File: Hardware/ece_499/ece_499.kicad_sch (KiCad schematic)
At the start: 3 parts, among them U1 ESP32-C3_SUPERMINI, U2 ATA6561-GAQW-N, U3 AP62200WU-7

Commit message: Continue components selection and setup
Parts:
- removed U1: ESP32-C3_SUPERMINI, ESP32-C3_SUPERMINI:MODULE_ESP32-C3_SUPERMINI, symbol Imported_Parts:ESP32-C3_SUPERMINI
- added D1: B5817W, Diode_THT:D_DO-41_SOD81_P10.16mm_Horizontal, symbol Diode:1N5817
- added Q1, Q2, Q3, Q4: DMN2004WK, Package_TO_SOT_SMD:SOT-323_SC-70, symbol Transistor_FET:2N7002H
- added U1: Xiao ESP32-C3, Imported_Parts:XIAO ESP32-C3, symbol Imported_Parts:XIAO_ESP32-C3
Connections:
- net +5V: now reaches U2.3 (VCC)
- net +5V: now also D1.2 (A)
- new net: D1.1 (K), U1.8 (VUSB)
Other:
- moved on the sheet: U3

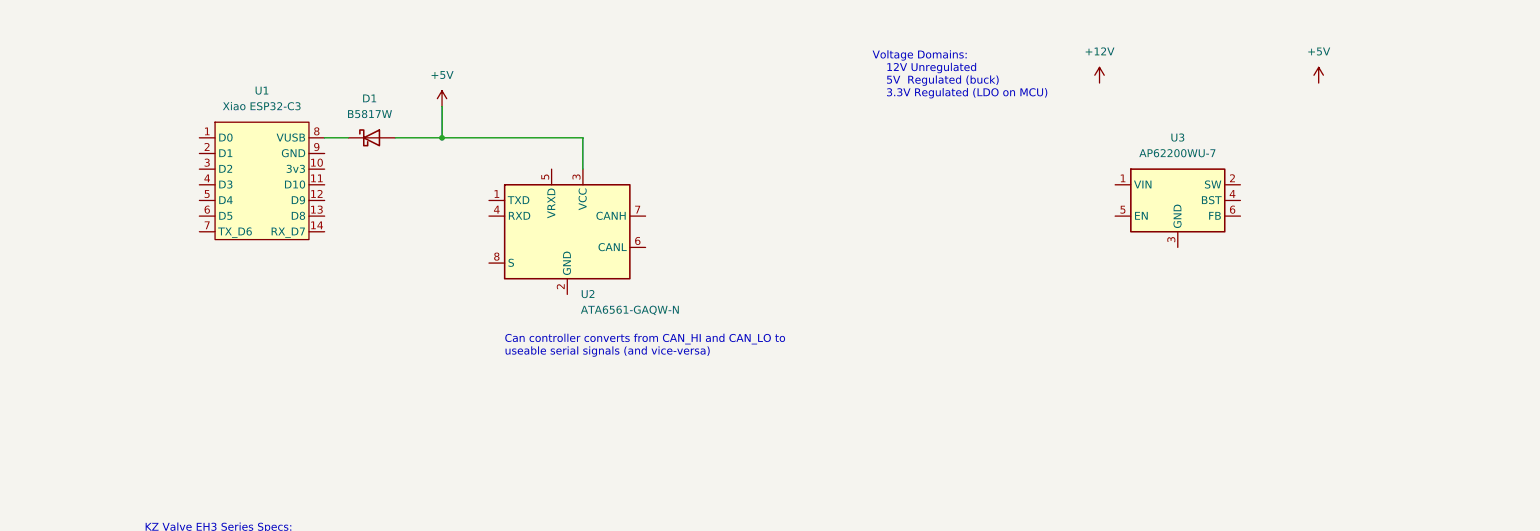
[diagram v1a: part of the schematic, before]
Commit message: Added parts
-Created circuit for regulator
-Wired up CAN transceiver
-Added rotary encoder
-Added I2C LCD interface
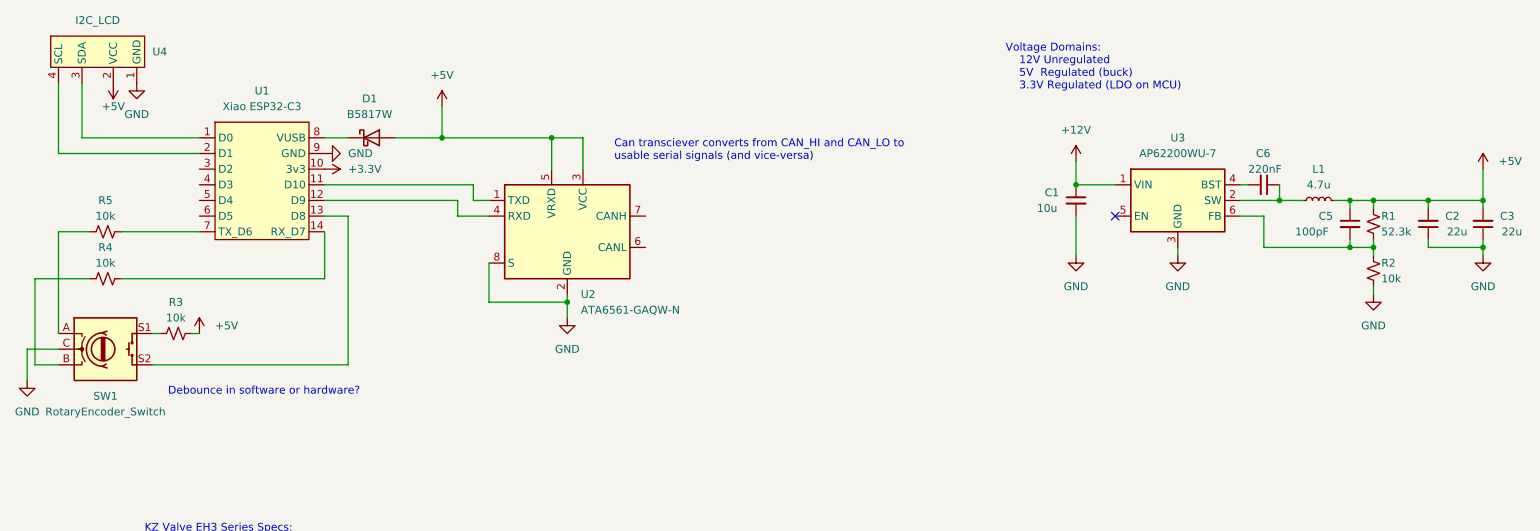
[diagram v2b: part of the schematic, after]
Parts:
- added C1: 10u, symbol Device:C_Small
- added C2, C3: 22u, symbol Device:C_Small
- added C5: 100pF, symbol Device:C_Small
- added C6: 220nF, symbol Device:C_Small
- added L1: 4.7u, symbol Device:L_Small
- added R1: 52.3k, symbol Device:R_Small_US
- added R2, R3, R4, R5: 10k, symbol Device:R_Small_US
- added SW1: RotaryEncoder_Switch, symbol Device:RotaryEncoder_Switch
- added U4: I2C_LCD, symbol Imported_Parts:I2C_LCD
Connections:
- net +12V: now also U3.1 (VIN), C1.1
- net +5V: now also U2.5 (VRXD), C2.2, C3.2, C5.1, L1.2, R1.1, R3.2, U4.2 (VCC)
- net at U1.1 (D0): now also U4.3 (SDA)
- net +3.3V: now reaches U1.10 (3v3)
- net at U1.11 (D10): now also U2.1 (TXD)
- net at U1.12 (D9): now also U2.4 (RXD)
- net at U1.13 (D8): now also SW1.S2
- net at U1.14 (RX_D7): now also R4.2
- net at U1.2 (D1): now also U4.4 (SCL)
- net at U1.7 (TX_D6): now also R5.2
- net GND: now reaches U1.9 (GND)
- net GND: now also U2.2 (GND), U2.8 (S), U3.3 (GND), C1.2, C2.1, C3.1, R2.2, SW1.C, U4.1 (GND)
- net at U3.2 (SW): now also C6.1, L1.1
- net at U3.4 (BST): now also C6.2
- net at U3.6 (FB): now also C5.2, R1.2, R2.1
- new net: R5.1, SW1.A
- new net: R3.1, SW1.S1
- new net: R4.1, SW1.B
- no-connect marks 0 -> 1
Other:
- note added: "Can transciever converts from CAN_HI and CAN_LO to usable serial signals (and vice-versa)"
- note added: "Debounce in software or hardware?"
- note removed: "Can controller converts from CAN_HI and CAN_LO to useable serial signals (and vice-versa)"

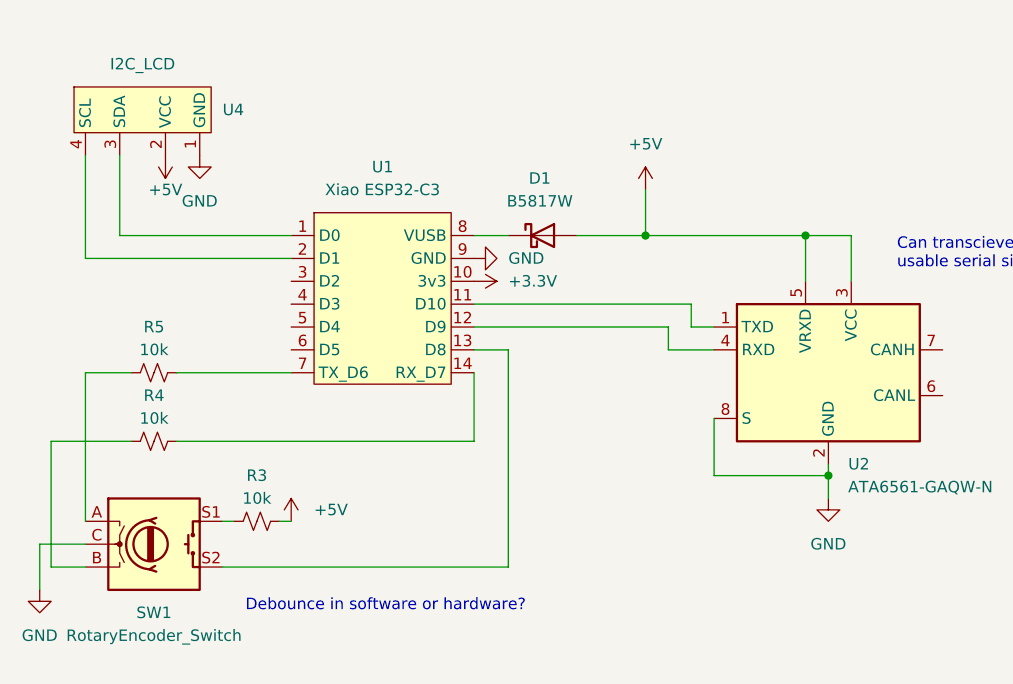
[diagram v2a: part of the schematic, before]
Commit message: stop being dumb
-fixed 5v into switch and can transceiver
-made the symbol less bad for the i2c
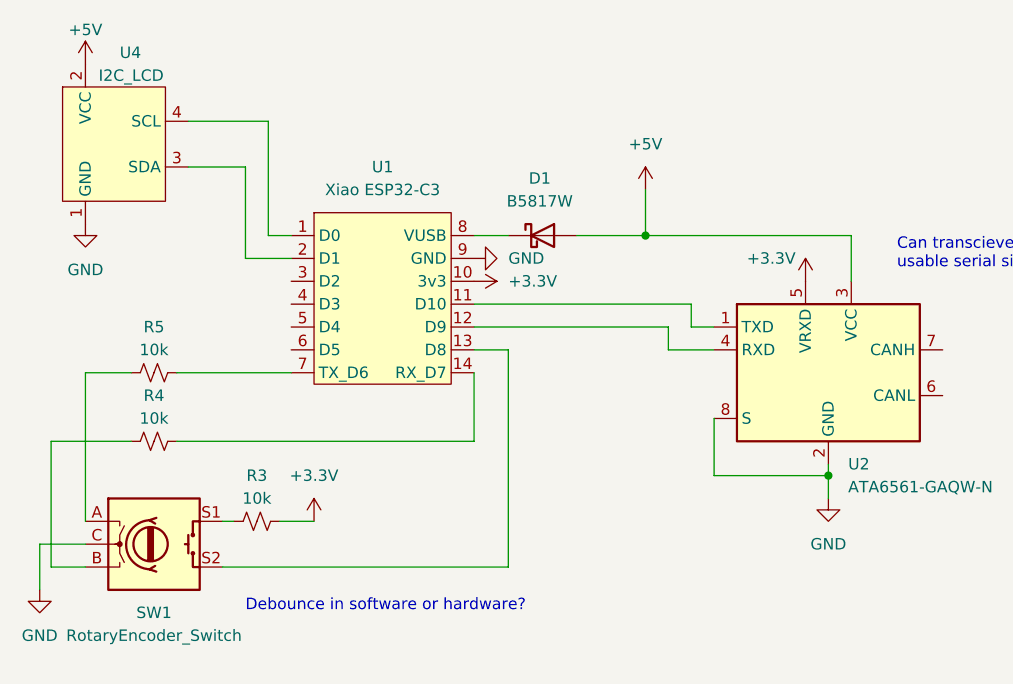
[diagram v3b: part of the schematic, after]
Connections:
- net +3.3V: now also R3.2, U2.5 (VRXD)
- net +5V: no longer R3.2, U2.5 (VRXD)
- net at U1.1 (D0): now also U4.4 (SCL); no longer U4.3 (SDA)
- net at U1.2 (D1): now also U4.3 (SDA); no longer U4.4 (SCL)
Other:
- moved on the sheet: U4
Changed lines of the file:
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@@
   (junction (at 224.79 53.34) (diameter 0) (color 0 0 0 0)
-  )
-  (junction (at 106.68 43.18) (diameter 0) (color 0 0 0 0)
   )
   (junction (at 240.03 60.96) (diameter 0) (color 0 0 0 0)
@@
     (stroke (width 0) (type default))
   )
-  (wire (pts (xy 88.9 43.18) (xy 106.68 43.18))
+  (wire (pts (xy 88.9 43.18) (xy 111.76 43.18))
+    (stroke (width 0) (type default))
+  )
+  (wire (pts (xy 44.45 45.72) (xy 49.53 45.72))
     (stroke (width 0) (type default))
   )
@@
     (stroke (width 0) (type default))
   )
+  (wire (pts (xy 44.45 35.56) (xy 44.45 45.72))
+    (stroke (width 0) (type default))
+  )
   (wire (pts (xy 69.85 43.18) (xy 73.66 43.18))
     (stroke (width 0) (type default))
@@
     (stroke (width 0) (type default))
   )
+  (wire (pts (xy 46.99 43.18) (xy 49.53 43.18))
+    (stroke (width 0) (type default))
+  )
   (wire (pts (xy 248.92 60.96) (xy 257.81 60.96))
     (stroke (width 0) (type default))
@@
     (stroke (width 0) (type default))
   )
-  (wire (pts (xy 30.48 34.29) (xy 30.48 43.18))
+  (wire (pts (xy 38.1 35.56) (xy 44.45 35.56))
     (stroke (width 0) (type default))
   )
@@
     (stroke (width 0) (type default))
   )
-  (wire (pts (xy 106.68 43.18) (xy 111.76 43.18))
-    (stroke (width 0) (type default))
-  )
   (wire (pts (xy 91.44 53.34) (xy 69.85 53.34))
     (stroke (width 0) (type default))
   )
-  (wire (pts (xy 26.67 45.72) (xy 49.53 45.72))
-    (stroke (width 0) (type default))
-  )
   (wire (pts (xy 257.81 60.96) (xy 257.81 59.69))
     (stroke (width 0) (type default))
@@
     (stroke (width 0) (type default))
   )
-  (wire (pts (xy 49.53 74.93) (xy 48.26 74.93))
+  (wire (pts (xy 52.07 74.93) (xy 48.26 74.93))
     (stroke (width 0) (type default))
   )
@@
     (stroke (width 0) (type default))
   )
-  (wire (pts (xy 26.67 34.29) (xy 26.67 45.72))
-    (stroke (width 0) (type default))
-  )
   (wire (pts (xy 240.03 60.96) (xy 240.03 62.23))
     (stroke (width 0) (type default))
@@
     (stroke (width 0) (type default))
   )
+  (wire (pts (xy 46.99 30.48) (xy 46.99 43.18))
+    (stroke (width 0) (type default))
+  )
+  (wire (pts (xy 38.1 30.48) (xy 46.99 30.48))
+    (stroke (width 0) (type default))
+  )
   (wire (pts (xy 96.52 55.88) (xy 91.44 55.88))
     (stroke (width 0) (type default))
@@
   )
   (wire (pts (xy 41.91 74.93) (xy 43.18 74.93))
-    (stroke (width 0) (type default))
-  )
-  (wire (pts (xy 30.48 43.18) (xy 49.53 43.18))
-    (stroke (width 0) (type default))
-  )
-  (wire (pts (xy 106.68 43.18) (xy 106.68 48.26))
     (stroke (width 0) (type default))
   )
@@
     )
   )
-  (symbol (lib_id "power:GND") (at 39.37 34.29 0) (unit 1)
-    (in_bom yes) (on_board yes) (dnp no) (fields_autoplaced)
-    (property "Reference" "#PWR013" (at 39.37 40.64 0)
-      (effects (font (size 1.27 1.27)) hide)
-    )
-    (property "Value" "GND" (at 39.37 39.37 0)
-      (effects (font (size 1.27 1.27)))
-    )
-    (property "Footprint" "" (at 39.37 34.29 0)
-      (effects (font (size 1.27 1.27)) hide)
-    )
-    (property "Datasheet" "" (at 39.37 34.29 0)
+  (symbol (lib_id "power:GND") (at 26.67 41.91 0) (unit 1)
+    (in_bom yes) (on_board yes) (dnp no) (fields_autoplaced)
+    (property "Reference" "#PWR013" (at 26.67 48.26 0)
+      (effects (font (size 1.27 1.27)) hide)
+    )
+    (property "Value" "GND" (at 26.67 46.99 0)
+      (effects (font (size 1.27 1.27)))
+    )
+    (property "Footprint" "" (at 26.67 41.91 0)
+      (effects (font (size 1.27 1.27)) hide)
+    )
+    (property "Datasheet" "" (at 26.67 41.91 0)
       (effects (font (size 1.27 1.27)) hide)
     )
@@
     )
   )
-  (symbol (lib_id "power:+5V") (at 35.56 34.29 180) (unit 1)
-    (in_bom yes) (on_board yes) (dnp no)
-    (property "Reference" "#PWR014" (at 35.56 30.48 0)
-      (effects (font (size 1.27 1.27)) hide)
-    )
-    (property "Value" "+5V" (at 35.56 38.1 0)
-      (effects (font (size 1.27 1.27)))
-    )
-    (property "Footprint" "" (at 35.56 34.29 0)
-      (effects (font (size 1.27 1.27)) hide)
-    )
-    (property "Datasheet" "" (at 35.56 34.29 0)
+  (symbol (lib_id "power:+3.3V") (at 106.68 48.26 0) (unit 1)
+    (in_bom yes) (on_board yes) (dnp no)
+    (property "Reference" "#PWR015" (at 106.68 52.07 0)
+      (effects (font (size 1.27 1.27)) hide)
+    )
+    (property "Value" "+3.3V" (at 102.87 45.72 0)
+      (effects (font (size 1.27 1.27)))
+    )
+    (property "Footprint" "" (at 106.68 48.26 0)
+      (effects (font (size 1.27 1.27)) hide)
+    )
+    (property "Datasheet" "" (at 106.68 48.26 0)
+      (effects (font (size 1.27 1.27)) hide)
+    )
+    (pin "1")
+    (instances
+      (project "ece_499"
+        (path "/3f2f140e-ca1f-4768-bf63-ce27bfebd1d1"
+          (reference "#PWR015") (unit 1)
+        )
+      )
+    )
+  )
+  (symbol (lib_id "power:+5V") (at 26.67 24.13 0) (unit 1)
+    (in_bom yes) (on_board yes) (dnp no)
+    (property "Reference" "#PWR014" (at 26.67 27.94 0)
+      (effects (font (size 1.27 1.27)) hide)
+    )
+    (property "Value" "+5V" (at 26.67 20.32 0)
+      (effects (font (size 1.27 1.27)))
+    )
+    (property "Footprint" "" (at 26.67 24.13 0)
+      (effects (font (size 1.27 1.27)) hide)
+    )
+    (property "Datasheet" "" (at 26.67 24.13 0)
       (effects (font (size 1.27 1.27)) hide)
     )
@@
     )
   )
-  (symbol (lib_id "Imported_Parts:I2C_LCD") (at 33.02 29.21 0) (unit 1)
-    (in_bom yes) (on_board yes) (dnp no)
-    (property "Reference" "U4" (at 41.91 29.21 0)
-      (effects (font (size 1.27 1.27)) (justify left))
-    )
-    (property "Value" "I2C_LCD" (at 33.02 24.13 0)
-      (effects (font (size 1.27 1.27)))
-    )
-    (property "Footprint" "" (at 30.48 29.21 0)
-      (effects (font (size 1.27 1.27)) hide)
-    )
-    (property "Datasheet" "" (at 30.48 29.21 0)
+  (symbol (lib_id "Imported_Parts:I2C_LCD") (at 29.21 33.02 0) (unit 1)
+    (in_bom yes) (on_board yes) (dnp no)
+    (property "Reference" "U4" (at 30.48 22.86 0)
+      (effects (font (size 1.27 1.27)) (justify left))
+    )
+    (property "Value" "I2C_LCD" (at 31.75 25.4 0)
+      (effects (font (size 1.27 1.27)))
+    )
+    (property "Footprint" "" (at 26.67 33.02 0)
+      (effects (font (size 1.27 1.27)) hide)
+    )
+    (property "Datasheet" "" (at 26.67 33.02 0)
       (effects (font (size 1.27 1.27)) hide)
     )
@@
         (path "/3f2f140e-ca1f-4768-bf63-ce27bfebd1d1"
           (reference "C3") (unit 1)
+        )
+      )
+    )
+  )
+  (symbol (lib_id "power:+3.3V") (at 52.07 74.93 0) (unit 1)
+    (in_bom yes) (on_board yes) (dnp no) (fields_autoplaced)
+    (property "Reference" "#PWR011" (at 52.07 78.74 0)
+      (effects (font (size 1.27 1.27)) hide)
+    )
+    (property "Value" "+3.3V" (at 52.07 69.85 0)
+      (effects (font (size 1.27 1.27)))
+    )
+    (property "Footprint" "" (at 52.07 74.93 0)
+      (effects (font (size 1.27 1.27)) hide)
+    )
+    (property "Datasheet" "" (at 52.07 74.93 0)
+      (effects (font (size 1.27 1.27)) hide)
+    )
+    (pin "1")
+    (instances
+      (project "ece_499"
+        (path "/3f2f140e-ca1f-4768-bf63-ce27bfebd1d1"
+          (reference "#PWR011") (unit 1)
         )
       )
@@
         )
       )
-    )
-  )
-  (symbol (lib_id "power:+5V") (at 49.53 74.93 0) (unit 1)
-    (in_bom yes) (on_board yes) (dnp no) (fields_autoplaced)
-    (property "Reference" "#PWR011" (at 49.53 78.74 0)
-      (effects (font (size 1.27 1.27)) hide)
-    )
-    (property "Value" "+5V" (at 52.07 73.66 0)
-      (effects (font (size 1.27 1.27)) (justify left))
-    )
-    (property "Footprint" "" (at 49.53 74.93 0)
-      (effects (font (size 1.27 1.27)) hide)
-    )
-    (property "Datasheet" "" (at 49.53 74.93 0)
-      (effects (font (size 1.27 1.27)) hide)
-    )
-    (pin "1")
-    (instances
-      (project "ece_499"
-        (path "/3f2f140e-ca1f-4768-bf63-ce27bfebd1d1"
-          (reference "#PWR011") (unit 1)
-        )
-      )
